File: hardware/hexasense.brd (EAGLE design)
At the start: 67 x 62 mm, 15 parts, among them IC1 AT45DB161D-SU

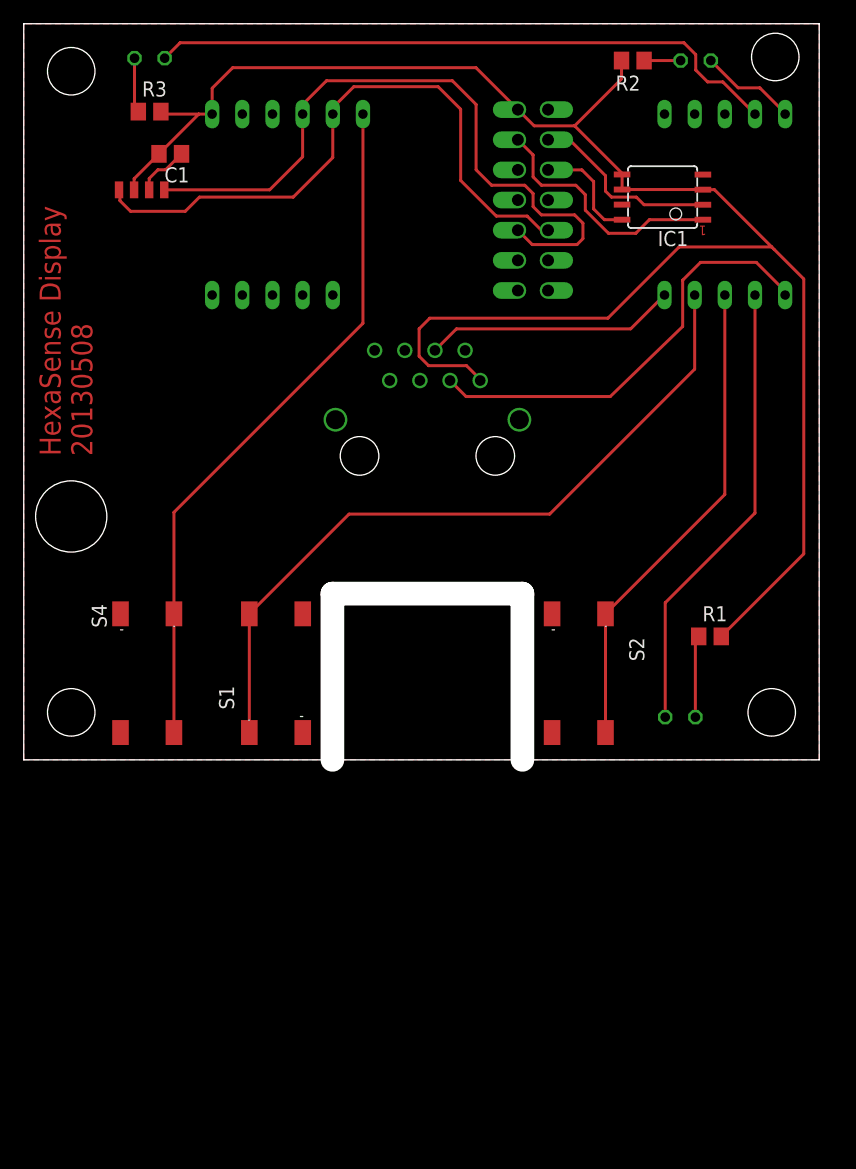
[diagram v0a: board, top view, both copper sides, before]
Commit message: added missing wires
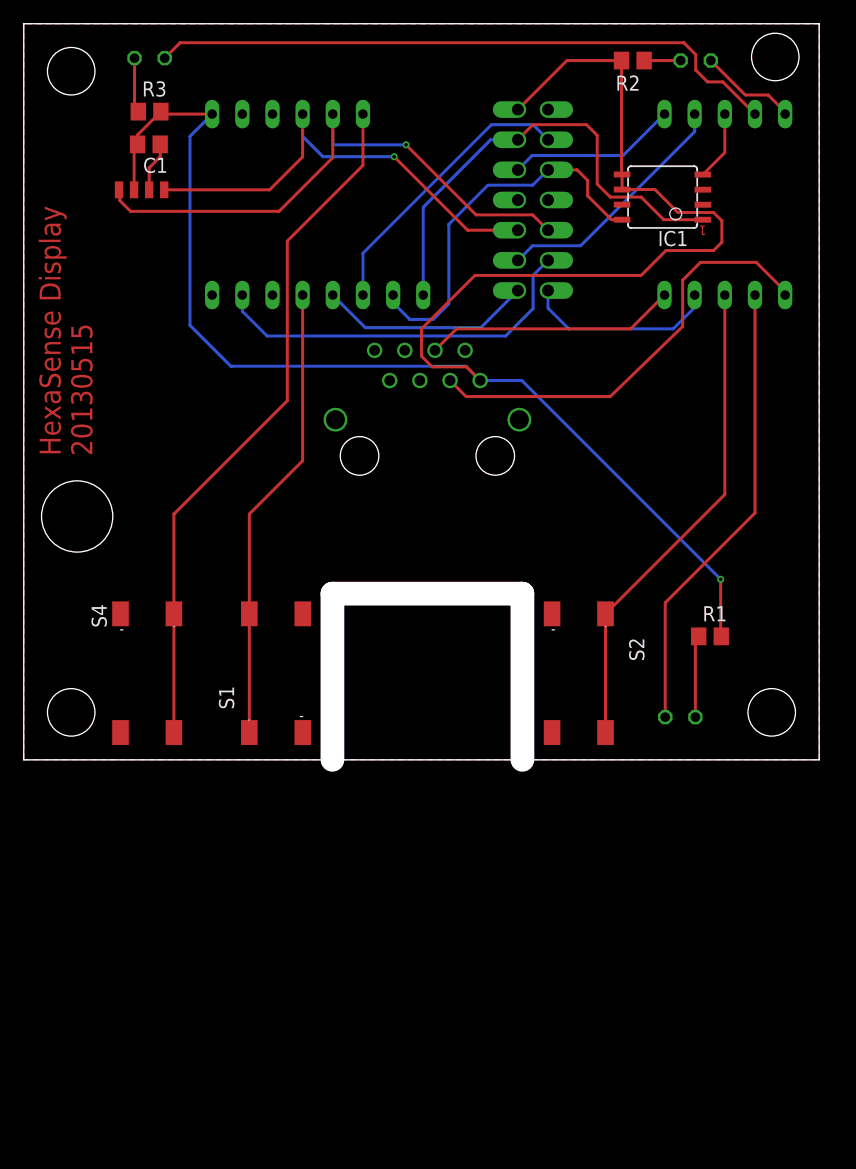
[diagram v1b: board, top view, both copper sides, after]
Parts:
- moved C1 1.97 mm to (10.5, 51.8)
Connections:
- removed net EPD-CSEL: U$2.P6
- removed net POWERCONTROL: U$2.P13
- removed net RESET: U$2.P12
- new net !RESET-FLASH: IC1.3
- new net N$8: U$4.PB2
- new net PWR_CTRL: U$2.P13, U$4.PA1
- new net RESET_DISP: U$2.P12, U$4.PA6
- new net SCLK: U$2.P3, U$4.SCLK
- new net SSEL: U$2.P6, U$4.PA5
- net +3V3: no longer IC1.3
- net CS: now also U$4.PA7
- net DISCHARGE: now also U$4.PB0
- net MISO: now also U$4.MISO
- net MOSI: now also U$4.MOSI
- net PWM: now also U$4.PB3
- net S1: now also U$4.PB1; no longer U$4.PA1
- net SCK: no longer U$2.P3
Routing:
- net PWM: track 0.00 -> 32.3 mm
- net SCLK: track 0.00 -> 24.1 mm
- net S1: track 62.3 -> 38.7 mm
- net MISO: track 9.32 -> 32.2 mm
- net RESET_DISP: track 0.00 -> 20.9 mm
- net MOSI: track 21.2 -> 39.6 mm
- net SDA: track 58.0 -> 39.7 mm, vias 0 -> 1
- net DISCHARGE: track 0.00 -> 18.0 mm
- net PWR_CTRL: track 0.00 -> 16.4 mm
- net SCK: track 16.1 -> 0.00 mm
- net SSEL: track 0.00 -> 14.3 mm
- net CS: track 0.00 -> 5.86 mm
- net SCL: track 52.7 -> 48.5 mm, vias 0 -> 1
- net +3V3: track 155.0 -> 157.9 mm, vias 0 -> 1
- added copper zone on layer 16, net N$4
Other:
- board text added: "HexaSense Display 20130515"
- board text removed: "HexaSense Display 20130508"

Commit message: added reset and SCLK line for flash chip
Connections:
- removed net SCK: IC1.2
- net !RESET-FLASH: now also U$4.PD4
- net SCLK: now also IC1.2
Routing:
- net !RESET-FLASH: track 0.00 -> 43.0 mm, vias 0 -> 1
- net SCLK: track 24.1 -> 40.9 mm, vias 0 -> 1
- net MISO: track 32.2 -> 31.4 mm
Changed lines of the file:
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@@
 <contactref element="S4" pad="4"/>
 <contactref element="IC1" pad="7"/>
-<polygon width="0.4064" layer="1">
+<polygon width="0.4064" layer="1" orphans="yes">
 <vertex x="0" y="0"/>
 <vertex x="67" y="0"/>
@@
 <contactref element="U$1" pad="7"/>
 </signal>
-<signal name="SCK">
-<contactref element="IC1" pad="2"/>
-</signal>
 <signal name="MISO">
 <contactref element="IC1" pad="8"/>
@@
 <contactref element="U$4" pad="MISO"/>
 <wire x1="50.396" y1="45.495" x2="49.505" y2="45.495" width="0.254" layer="1"/>
-<wire x1="49.505" y1="45.495" x2="47.5" y2="47.5" width="0.254" layer="1"/>
-<wire x1="47.5" y1="47.5" x2="47.5" y2="48.8" width="0.254" layer="1"/>
-<wire x1="47.5" y1="48.8" x2="46.61" y2="49.69" width="0.254" layer="1"/>
-<wire x1="46.61" y1="49.69" x2="44.16" y2="49.69" width="0.254" layer="1"/>
 <wire x1="44.16" y1="49.69" x2="42.87" y2="48.4" width="0.254" layer="16"/>
 <wire x1="42.87" y1="48.4" x2="39.1" y2="48.4" width="0.254" layer="16"/>
@@
 <wire x1="32.5" y1="37.1" x2="31.11" y2="38.49" width="0.254" layer="16"/>
 <wire x1="31.11" y1="38.49" x2="31.11" y2="39.15" width="0.254" layer="16"/>
+<wire x1="44.16" y1="49.69" x2="45.31" y2="49.69" width="0.254" layer="1"/>
+<wire x1="45.31" y1="49.69" x2="49.505" y2="45.495" width="0.254" layer="1"/>
 </signal>
 <signal name="MOSI">
@@
 <signal name="!RESET-FLASH">
 <contactref element="IC1" pad="3"/>
+<contactref element="U$4" pad="PD4"/>
+<wire x1="57.204" y1="48.025" x2="54.975" y2="48.025" width="0.254" layer="1"/>
+<wire x1="54.975" y1="48.025" x2="52.2" y2="50.8" width="0.254" layer="1"/>
+<wire x1="52.2" y1="50.8" x2="52.2" y2="54" width="0.254" layer="1"/>
+<wire x1="52.2" y1="54" x2="51.5" y2="54.7" width="0.254" layer="1"/>
+<via x="51.5" y="54.7" extent="1-16" drill="0.3"/>
+<wire x1="51.5" y1="54.7" x2="49.1" y2="57.1" width="0.254" layer="16"/>
+<wire x1="49.1" y1="57.1" x2="23.66" y2="57.1" width="0.254" layer="16"/>
+<wire x1="23.66" y1="57.1" x2="20.95" y2="54.39" width="0.254" layer="16"/>
 </signal>
 <signal name="SCLK">
@@
 <wire x1="39.4" y1="53.5" x2="28.57" y2="42.67" width="0.254" layer="16"/>
 <wire x1="28.57" y1="42.67" x2="28.57" y2="39.15" width="0.254" layer="16"/>
+<contactref element="IC1" pad="2"/>
+<wire x1="57.204" y1="46.755" x2="55.345" y2="46.755" width="0.254" layer="1"/>
+<wire x1="55.345" y1="46.755" x2="51.2" y2="50.9" width="0.254" layer="1"/>
+<wire x1="51.2" y1="50.9" x2="51.2" y2="52.7" width="0.254" layer="1"/>
+<via x="51.2" y="52.7" extent="1-16" drill="0.3"/>
+<wire x1="51.2" y1="52.7" x2="44.63" y2="52.7" width="0.254" layer="16"/>
+<wire x1="44.63" y1="52.7" x2="44.16" y2="52.23" width="0.254" layer="16"/>
 </signal>
 <signal name="BUSY">
@@
 </signal>
 <signal name="N$4">
-<polygon width="0.254" layer="16">
+<polygon width="0.254" layer="16" orphans="yes">
 <vertex x="0" y="0"/>
 <vertex x="67" y="0"/>

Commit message: added testpads to schematic
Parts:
- added TP1, TP2, TP3, TP4, TP5, TP6, TP7, TP8: TPB1,27, testpad:B1,27
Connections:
- net !RESET-FLASH: now also TP3.TP
- net +3V3: now also TP5.TP, TP6.TP
- net CS: now also TP4.TP
- net GND: now also TP7.TP
- net MISO: now also TP8.TP
- net MOSI: now also TP1.TP
- net SCLK: now also TP2.TP
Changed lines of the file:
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@@
 <element name="LED3" library="led" package="LED3MM" value="" x="10.6" y="59.1" rot="MR180"/>
 <element name="U$2" library="epaper" package="EPAPER" value="EPAPER" x="34" y="46"/>
+<element name="TP1" library="testpad" package="B1,27" value="TPB1,27" x="1" y="-3.8">
+<attribute name="TP_SIGNAL_NAME" value="" x="1" y="-3.8" size="1.778" layer="27" display="off"/>
+</element>
+<element name="TP2" library="testpad" package="B1,27" value="TPB1,27" x="1" y="-7.8">
+<attribute name="TP_SIGNAL_NAME" value="" x="1" y="-7.8" size="1.778" layer="27" display="off"/>
+</element>
+<element name="TP3" library="testpad" package="B1,27" value="TPB1,27" x="1" y="-11.8">
+<attribute name="TP_SIGNAL_NAME" value="" x="1" y="-11.8" size="1.778" layer="27" display="off"/>
+</element>
+<element name="TP4" library="testpad" package="B1,27" value="TPB1,27" x="1" y="-15.8">
+<attribute name="TP_SIGNAL_NAME" value="" x="1" y="-15.8" size="1.778" layer="27" display="off"/>
+</element>
+<element name="TP5" library="testpad" package="B1,27" value="TPB1,27" x="1" y="-19.8">
+<attribute name="TP_SIGNAL_NAME" value="" x="1" y="-19.8" size="1.778" layer="27" display="off"/>
+</element>
+<element name="TP6" library="testpad" package="B1,27" value="TPB1,27" x="1" y="-23.8">
+<attribute name="TP_SIGNAL_NAME" value="" x="1" y="-23.8" size="1.778" layer="27" display="off"/>
+</element>
+<element name="TP7" library="testpad" package="B1,27" value="TPB1,27" x="1" y="-27.8">
+<attribute name="TP_SIGNAL_NAME" value="" x="1" y="-27.8" size="1.778" layer="27" display="off"/>
+</element>
+<element name="TP8" library="testpad" package="B1,27" value="TPB1,27" x="1" y="-31.8">
+<attribute name="TP_SIGNAL_NAME" value="" x="1" y="-31.8" size="1.778" layer="27" display="off"/>
+</element>
 </elements>
 <signals>
@@
 <contactref element="U$2" pad="P1"/>
 <contactref element="U$2" pad="P1"/>
+<contactref element="TP7" pad="TP"/>
+<wire x1="8.15" y1="2.3" x2="1" y2="-27.8" width="0" layer="19" extent="1-1"/>
 </signal>
 <signal name="+3V3">
@@
 <wire x1="58.7" y1="15.2" x2="58.7" y2="10.45" width="0.254" layer="1"/>
 <wire x1="58.7" y1="10.45" x2="58.75" y2="10.4" width="0.254" layer="1"/>
+<contactref element="TP5" pad="TP"/>
+<contactref element="TP6" pad="TP"/>
+<wire x1="1" y1="-19.8" x2="17.45" y2="33.15" width="0" layer="19" extent="1-16"/>
+<wire x1="1" y1="-23.8" x2="1" y2="-19.8" width="0" layer="19" extent="1-1"/>
 </signal>
 <signal name="TEMP_1">
@@
 <wire x1="44.16" y1="49.69" x2="45.31" y2="49.69" width="0.254" layer="1"/>
 <wire x1="45.31" y1="49.69" x2="49.505" y2="45.495" width="0.254" layer="1"/>
+<contactref element="TP8" pad="TP"/>
+<wire x1="1" y1="-31.8" x2="32.5" y2="37.1" width="0" layer="19" extent="1-16"/>
 </signal>
 <signal name="MOSI">
@@
 <wire x1="39.33" y1="52.23" x2="33.65" y2="46.55" width="0.254" layer="16"/>
 <wire x1="33.65" y1="46.55" x2="33.65" y2="39.15" width="0.254" layer="16"/>
+<contactref element="TP1" pad="TP"/>
+<wire x1="1" y1="-3.8" x2="33.65" y2="39.15" width="0" layer="19" extent="1-1"/>
 </signal>
 <signal name="CS">
@@
 <wire x1="57.204" y1="49.295" x2="59.05" y2="51.141" width="0.254" layer="1"/>
 <wire x1="59.05" y1="51.141" x2="59.05" y2="54.39" width="0.254" layer="1"/>
+<contactref element="TP4" pad="TP"/>
+<wire x1="1" y1="-15.8" x2="57.204" y2="49.295" width="0" layer="19" extent="1-1"/>
 </signal>
 <signal name="N$1">
@@
 <wire x1="49.1" y1="57.1" x2="23.66" y2="57.1" width="0.254" layer="16"/>
 <wire x1="23.66" y1="57.1" x2="20.95" y2="54.39" width="0.254" layer="16"/>
+<contactref element="TP3" pad="TP"/>
+<wire x1="1" y1="-11.8" x2="20.95" y2="54.39" width="0" layer="19" extent="1-1"/>
 </signal>
 <signal name="SCLK">
@@
 <wire x1="51.2" y1="52.7" x2="44.63" y2="52.7" width="0.254" layer="16"/>
 <wire x1="44.63" y1="52.7" x2="44.16" y2="52.23" width="0.254" layer="16"/>
+<contactref element="TP2" pad="TP"/>
+<wire x1="1" y1="-7.8" x2="28.57" y2="39.15" width="0" layer="19" extent="1-1"/>
 </signal>
 <signal name="BUSY">

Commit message: testpads and placement print
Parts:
- removed TP1, TP2, TP3, TP4, TP5, TP6, TP7, TP8: TPB1,27, testpad:B1,27
- added !RESET, CS, GND, MISO, MOSI, SCLK, VCC: TPB1,27, testpad:B1,27
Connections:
- net !RESET-FLASH: now also !RESET.TP; no longer TP3.TP
- net +3V3: now also VCC.TP; no longer TP5.TP, TP6.TP
- net CS: now also CS.TP; no longer TP4.TP
- net GND: now also GND.TP; no longer TP7.TP
- net MISO: now also MISO.TP; no longer TP8.TP
- net MOSI: now also MOSI.TP; no longer TP1.TP
- net SCLK: now also SCLK.TP; no longer TP2.TP
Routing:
- net SCLK: track 40.9 -> 45.1 mm
- net !RESET-FLASH: track 43.0 -> 46.9 mm
- net CS: track 5.86 -> 8.76 mm
- net MOSI: track 39.6 -> 42.1 mm
- net MISO: track 31.4 -> 33.9 mm
- net +3V3: track 157.9 -> 160.3 mm
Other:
- board text added: "HexaSense Display 20130617"
- board text removed: "HexaSense Display 20130515"

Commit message: several minor changes
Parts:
- turned C1 to 180 degrees
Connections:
- removed net DATA: U$4.PD3
- removed net N$8: U$4.PB2
- net BUSY: now also U$4.PD3
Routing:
- net BUSY: track 0.00 -> 31.8 mm
- net GND: track 4.21 -> 3.16 mm, vias 0 -> 5
- net MISO: track 33.9 -> 34.9 mm
- net SCLK: track 45.1 -> 44.5 mm
- added copper zone on layer 16, net GND
- removed copper zone on layer 16, net N$4
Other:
- board text added: "HexaSense Display 20130619"
- board text removed: "HexaSense Display 20130617"
